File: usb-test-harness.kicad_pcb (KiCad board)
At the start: 4 copper layers, 98 x 85 mm, 92 parts, among them J1 Conn_01x06, J10 USB_A_DUAL, J4 USB_A (female down), J5 Conn_01x03_Male, J6 USB_A_DUAL, J7 USB_A_DUAL, J8 USB_A male UP, J9 USB_B_Micro (up), U1 2k i2c eeprom, U10 NUP4202, U11 NUP4202, U12 NUP4202, U2 SE5120ST33, U3 USB2517, U4 APL3511C, U5 APL3511C, U6 APL3511C, U7 APL3511C, U8 APL3511C, U9 APL3511C, Y1 24MHz

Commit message: last update before changing box design
original box is lovely, and cheap, but only available on TME, so we've
found a new box, Bud CU-388, available on dk and mouser as well, at a
nearly as good price.
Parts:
- moved U10 124.5 mm to (115.2, 66.2)
- moved U11 124.5 mm to (115.2, 70.0)
- moved U12 124.5 mm to (119.5, 66.2)
- moved H5 105.9 mm to (124.9, 66.3)
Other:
- board text added: "github.com/karlp/hubbish rev 2020-03"

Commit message: Updated "finished" for new bud cu-388 box
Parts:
- removed H5: MountingHole, MountingHole:MountingHole_4mm
- moved D1 48.8 mm to (95.2, 57.0)
- moved D2 48.8 mm to (95.2, 55.3)
- moved U10 45.3 mm to (78.2, 40.1)
- moved U12 45.3 mm to (82.5, 40.1)
- moved U11 45.3 mm to (78.2, 44.0)
- moved D9 30.3 mm to (180.8, 94.3)
- moved C21 26.4 mm to (167.8, 95.3)
- moved C30 25.1 mm to (99.7, 97.9), turned to 180 degrees
- moved H4 24.8 mm to (185.3, 105.4)
- moved R10 24.7 mm to (165.0, 59.2), turned to 180 degrees
- moved JP1 24.6 mm to (164.0, 55.0), turned to 180 degrees
- moved H2 24.0 mm to (105.1, 105.4)
- moved J10 23.8 mm to (170.3, 104.4)
- moved U5 23.6 mm to (171.3, 95.3)
- moved U4 23.5 mm to (169.0, 99.2)
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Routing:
- net +5V: track 112.0 -> 41.0 mm
- net +3V3: track 141.1 -> 109.9 mm
- net GNDPWR: track 334.6 -> 306.7 mm, vias 0 -> 1
- net GND: track 67.5 -> 47.1 mm, vias 54 -> 50
- net /upstream-config-leds/CFG_SEL1: track 83.3 -> 98.5 mm, vias 2 -> 0
- net /upstream-config-leds/LED_A3: track 67.1 -> 78.1 mm
- net /upstream-config-leds/~RESET: track 15.5 -> 26.2 mm
- net /upstream-config-leds/LED_A6: track 90.4 -> 80.1 mm
- net /downstream-port-power/OC5: track 93.2 -> 84.0 mm
- net /downstream-port-power/VBUS6: track 17.8 -> 26.9 mm
- net /upstream-config-leds/CFG_SEL1_A: track 9.15 -> 18.2 mm
- net /upstream-config-leds/LA_3-1: track 13.3 -> 4.34 mm
- net /downstream-port-power/EN5: track 97.0 -> 88.1 mm
- net /upstream-config-leds/CFG_SEL2: track 48.7 -> 40.1 mm
- net /downstream-port-power/EN6: track 81.1 -> 74.0 mm
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- removed copper zone on F.Cu, net +5V
- removed copper zone on B.Cu, net GND
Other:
- board size 98 x 85 mm -> 103.6 x 71.8 mm
- board text added: "0"
- board text added: "1"
- board text added: "2"
- board text removed: "2 1 0"

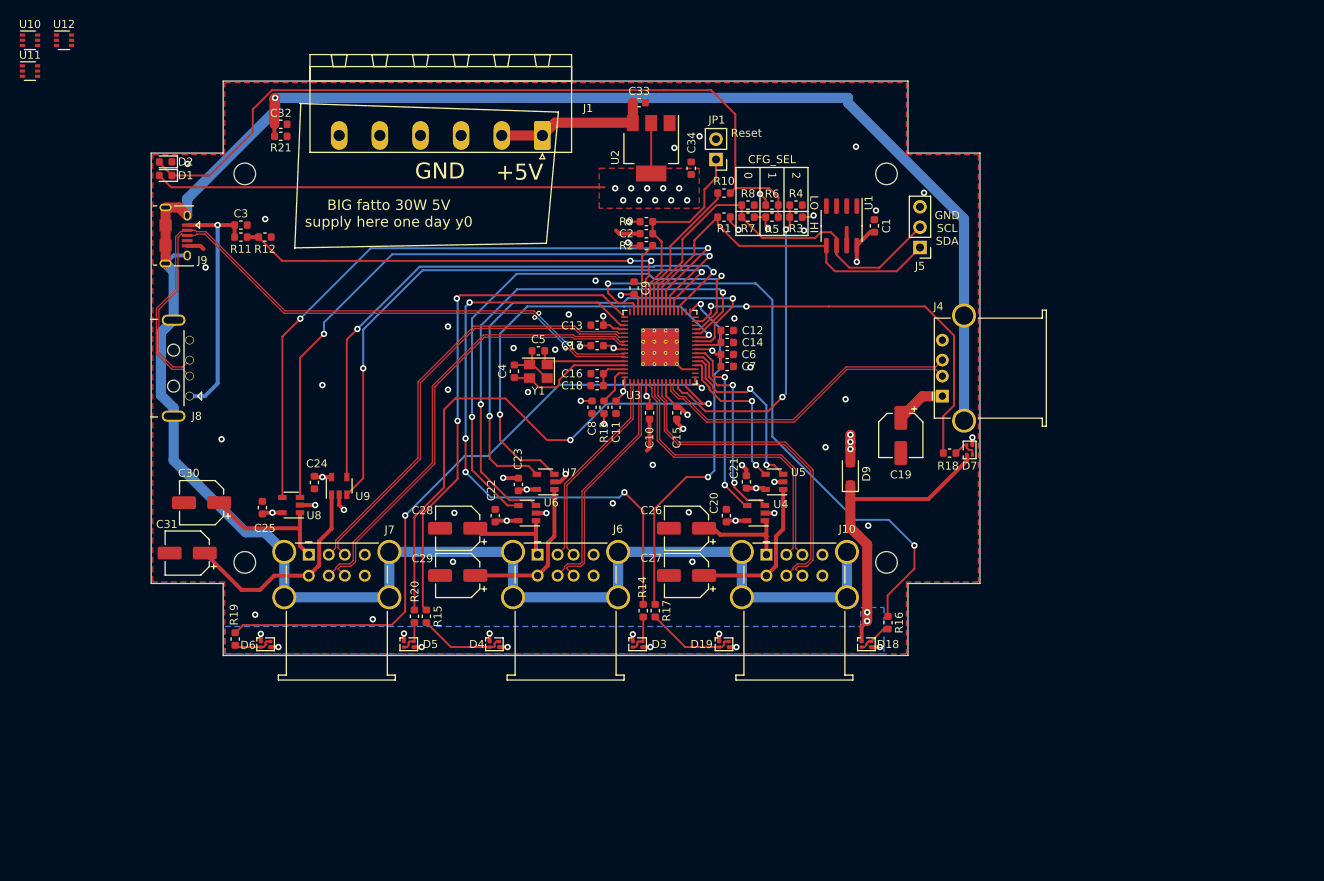
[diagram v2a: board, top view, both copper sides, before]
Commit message: Added esd protection.
Still haven't re-routed the upstream side yet, but nearly.
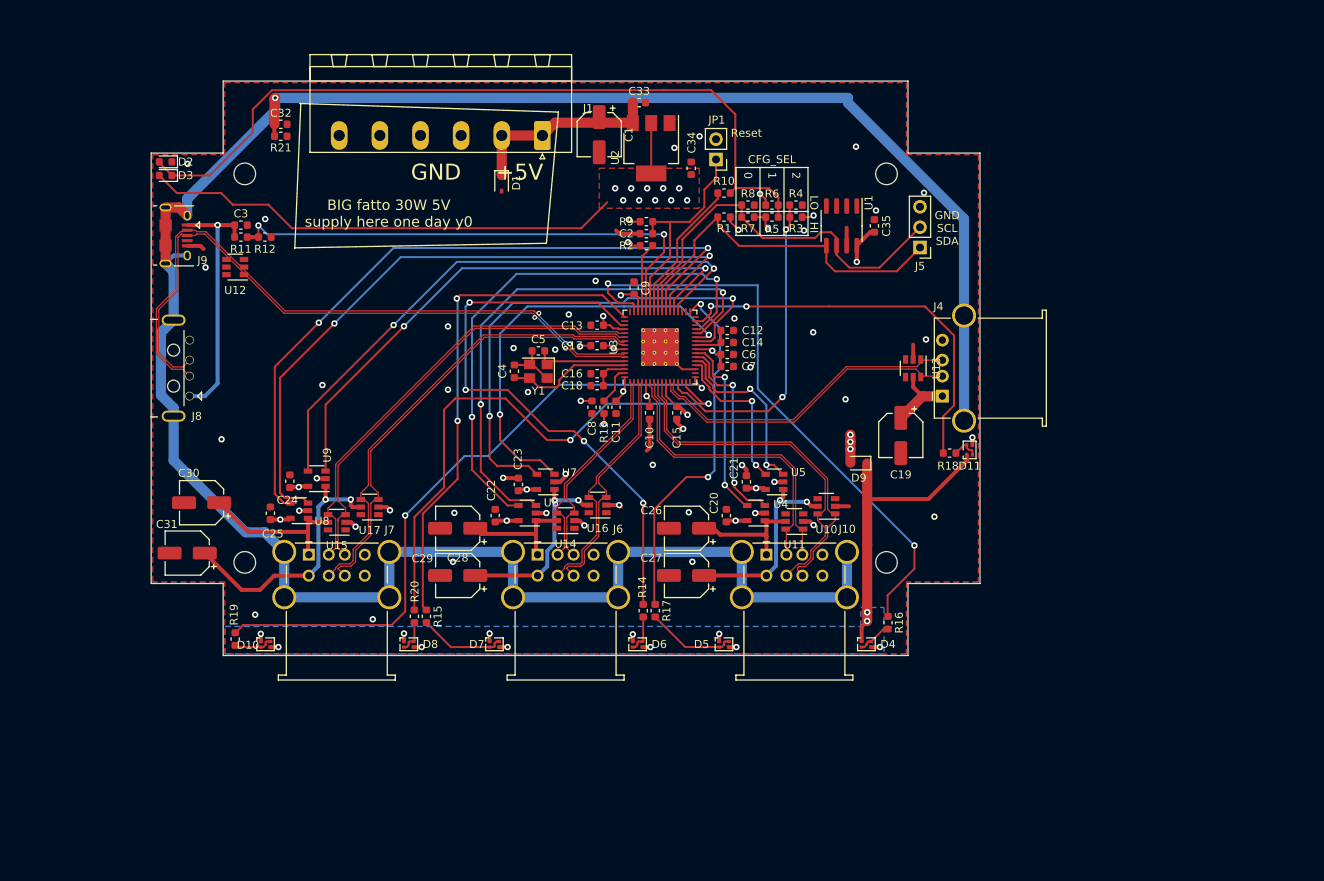
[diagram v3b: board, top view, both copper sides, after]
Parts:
- added C1: 100uF, Capacitor_SMD:CP_Elec_5x5.4, F.Cu at (149.4, 51.9)
- added D1: SD05-7, Diode_SMD:D_SOD-323, F.Cu at (137.2, 57.9)
- added U13: NUP4202, Package_TO_SOT_SMD:SOT-23-6, F.Cu at (188.7, 81.1)
- added U14: NUP4202, Package_TO_SOT_SMD:SOT-23-6, F.Cu at (145.2, 100.2)
- added U15: NUP4202, Package_TO_SOT_SMD:SOT-23-6, F.Cu at (116.6, 100.3)
- added U16: NUP4202, Package_TO_SOT_SMD:SOT-23-6, F.Cu at (149.2, 98.2)
- added U17: NUP4202, Package_TO_SOT_SMD:SOT-23-6, F.Cu at (120.7, 98.5)
- D9: footprint Diode_SMD:D_SOD-123F -> Diode_SMD:D_SOD-323
- U10, U11, U12: footprint Package_TO_SOT_SMD:SOT-363_SC-70-6 -> Package_TO_SOT_SMD:SOT-23-6
- moved U10 115.3 mm to (177.8, 98.3), turned to 180 degrees
- moved U11 110.9 mm to (173.8, 100.2), turned to 180 degrees
- moved U12 35.5 mm to (103.9, 68.5), turned to 180 degrees
- moved C24 3.07 mm to (110.7, 95.2), turned to 90 degrees
- moved U9 2.94 mm to (114.1, 94.9), turned to 180 degrees
- moved D9 1.71 mm to (181.8, 93.0), turned to 180 degrees
- moved C25 1.22 mm to (108.3, 99.2)
- moved U8 1.22 mm to (111.9, 98.9)
- renumbered C1 to C35, D6 to D10, D7 to D11, D1 to D3, D18 to D4, D19 to D5, D3 to D6, D4 to D7, D5 to D8
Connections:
- U10 pad 1: (no net) -> /downstream-port-power/U2+
- U10 pad 2: (no net) -> GND
- U10 pad 5: (no net) -> /downstream-port-power/VBUS2
- U10 pad 6: (no net) -> /downstream-port-power/U2-
- U11 pad 1: (no net) -> /downstream-port-power/U1+
- U11 pad 2: (no net) -> GND
- U11 pad 5: (no net) -> /downstream-port-power/VBUS1
- U11 pad 6: (no net) -> /downstream-port-power/U1-
- U12 pad 1: (no net) -> /upstream-config-leds/UP+
- U12 pad 2: (no net) -> GND
- U12 pad 3: (no net) -> /upstream-config-leds/UP-
- U12 pad 4: (no net) -> /upstream-config-leds/UP-
- U12 pad 5: (no net) -> /upstream-config-leds/VBUS_UP
- U12 pad 6: (no net) -> /upstream-config-leds/UP+
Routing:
- net GND: track 47.1 -> 56.8 mm, vias 50 -> 55
- net +5V: track 41.0 -> 49.7 mm
- net /upstream-config-leds/VBUS_DET: track 58.4 -> 64.8 mm
- net /downstream-port-power/VBUS6: track 26.9 -> 32.9 mm, vias 0 -> 2
- net /upstream-config-leds/LED_A1: track 78.4 -> 72.6 mm
- net /downstream-port-power/VBUS2: track 18.1 -> 23.1 mm, vias 0 -> 2
- net /downstream-port-power/VBUS4: track 19.5 -> 24.0 mm, vias 0 -> 2
- net +3V3: track 109.9 -> 113.9 mm
- net /downstream-port-power/OC5: track 84.0 -> 87.8 mm
- net /downstream-port-power/OC6: track 73.4 -> 69.9 mm
- net /downstream-port-power/U2-: track 41.7 -> 44.8 mm
- net /downstream-port-power/VBUS5: track 17.3 -> 20.1 mm
- net /downstream-port-power/VBUS1: track 11.3 -> 13.9 mm
- net /downstream-port-power/VBUS3: track 12.3 -> 14.8 mm
- net /downstream-port-power/U2+: track 41.7 -> 44.2 mm
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
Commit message: "finished" upstream ESD, silk, text and commentary
Nearly there?
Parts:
- moved U12 4.70 mm to (102.0, 64.2), turned to 90 degrees
- moved R19 4.00 mm to (107.4, 113.0), turned to 180 degrees
- moved C3 3.49 mm to (107.4, 61.0)
- moved R11 3.49 mm to (107.4, 62.5)
- moved R12 3.49 mm to (110.4, 62.5)
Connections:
- U12 pad 1: /upstream-config-leds/UP+ -> (no net)
- U12 pad 3: /upstream-config-leds/UP- -> /upstream-config-leds/UP+
- U12 pad 6: /upstream-config-leds/UP+ -> (no net)
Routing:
- net /upstream-config-leds/LED_A6: track 80.1 -> 75.4 mm
- net /upstream-config-leds/VBUS_UP: track 31.4 -> 36.0 mm
- net GND: track 56.8 -> 60.9 mm, vias 55 -> 58
- net +3V3: track 113.9 -> 111.2 mm
- net /upstream-config-leds/VBUS_DET: track 64.8 -> 62.9 mm
- net /upstream-config-leds/LA_6-6: track 4.98 -> 6.28 mm
- net /upstream-config-leds/UP-: track 84.2 -> 85.4 mm
- net /upstream-config-leds/UP+: track 83.2 -> 84.4 mm
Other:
- board text added: "HiSpeed"
- board text added: "Port 1/2"
- board text added: "Port 3/4"
- board text added: "Port 5"
- board text added: "Port 6/7"
- board text added: "Port LEDs Green: LS Red: FS Orange: HS"
- board text added: "Upstream"

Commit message: more silk and polish tweaks
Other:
- board text removed: "FIX ALL THE FUCKING SILK!"

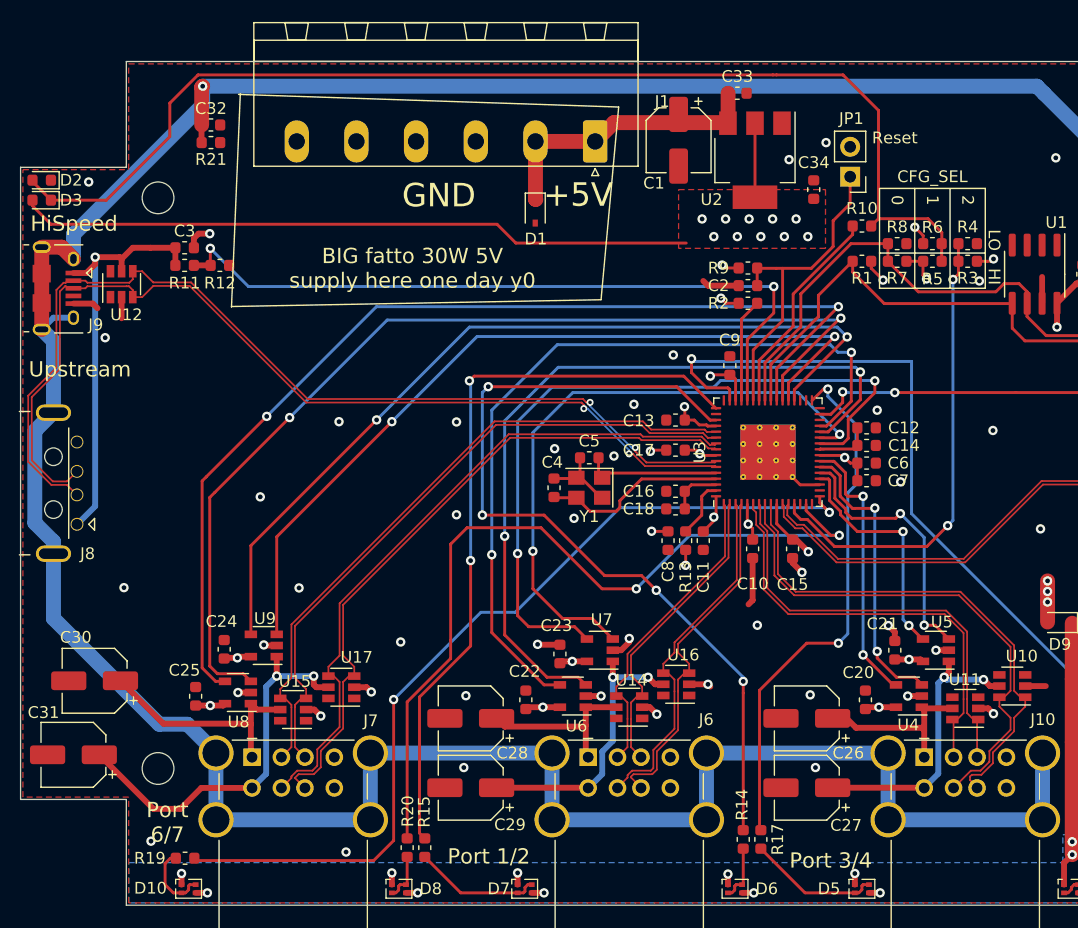
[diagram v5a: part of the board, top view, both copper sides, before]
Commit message: pcb: expand usb hub vias to 0.4mm for cheaper manufacturing
also, added jlc text for pcb order number
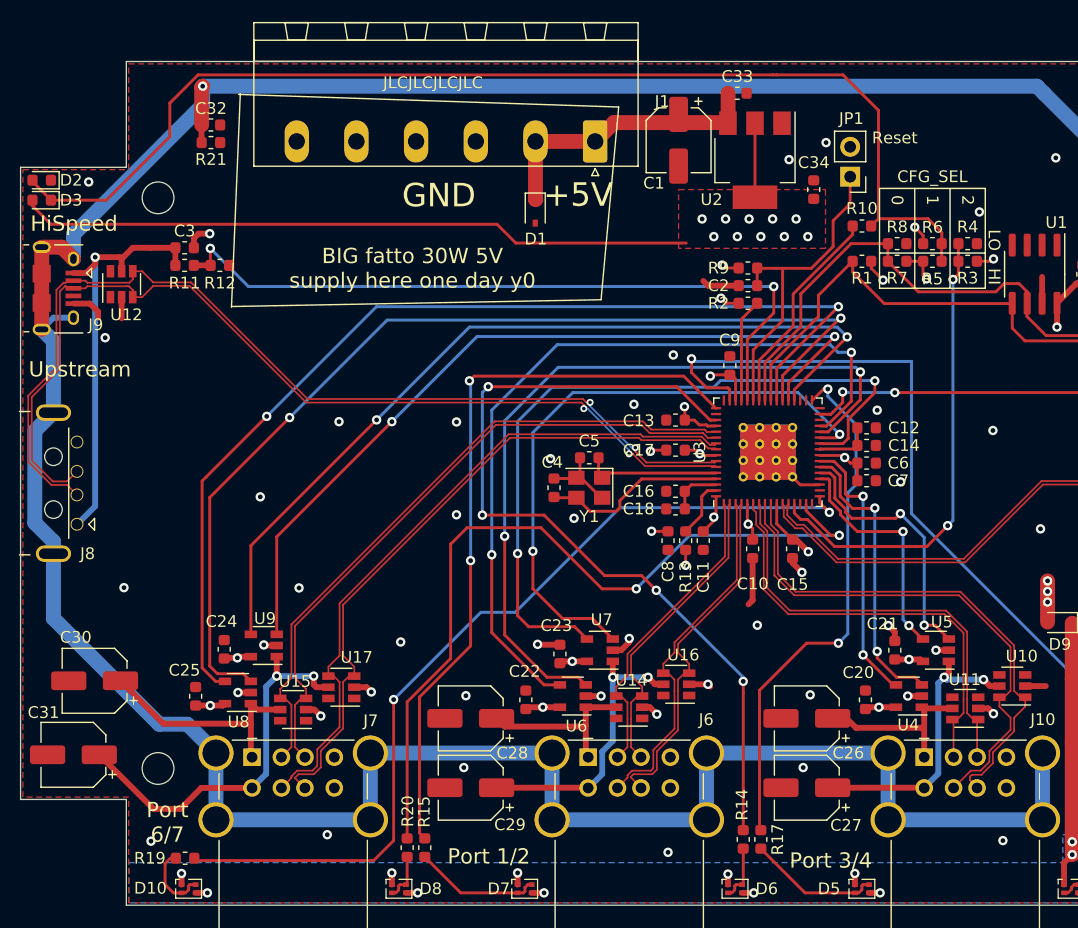
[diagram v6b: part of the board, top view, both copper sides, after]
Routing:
- net GND: track 60.9 -> 61.6 mm, vias 58 -> 59
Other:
- board text added: "JLCJLCJLCJLC"

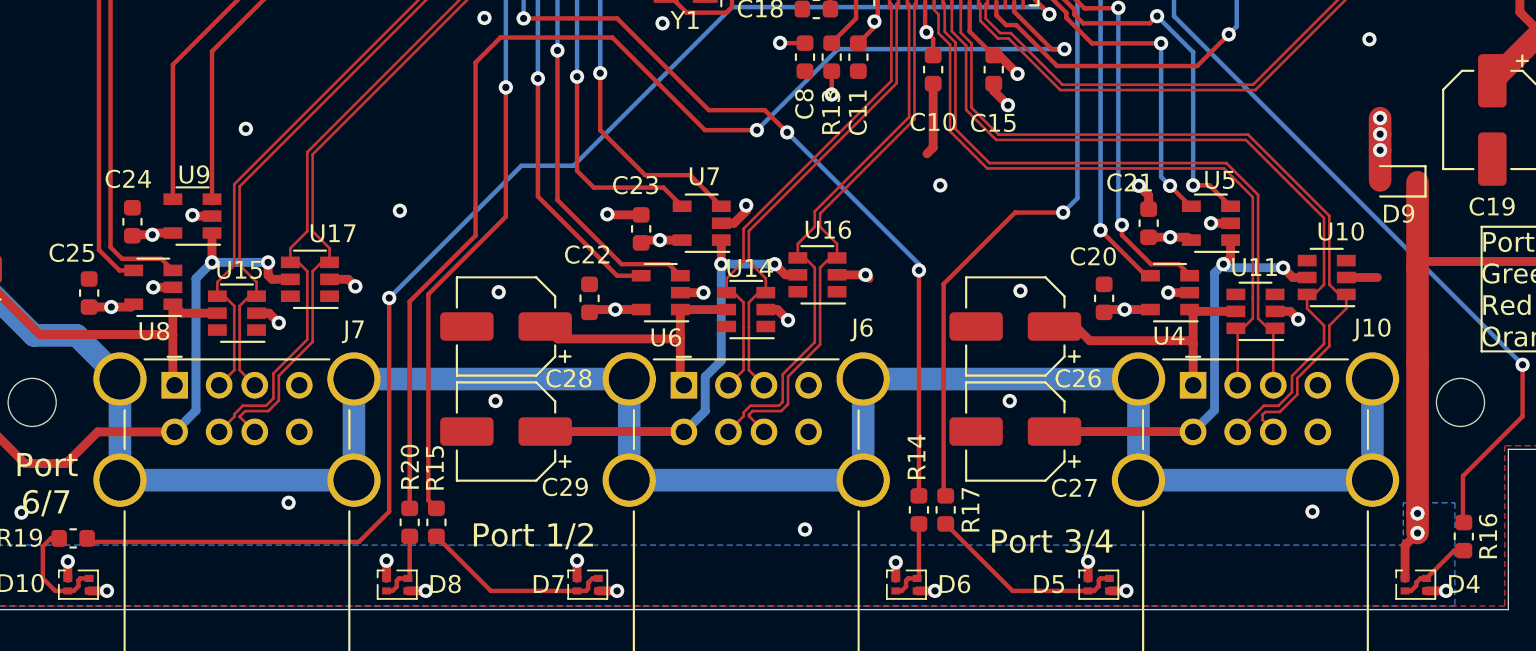
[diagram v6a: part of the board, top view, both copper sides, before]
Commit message: update pcb to latest proj version too
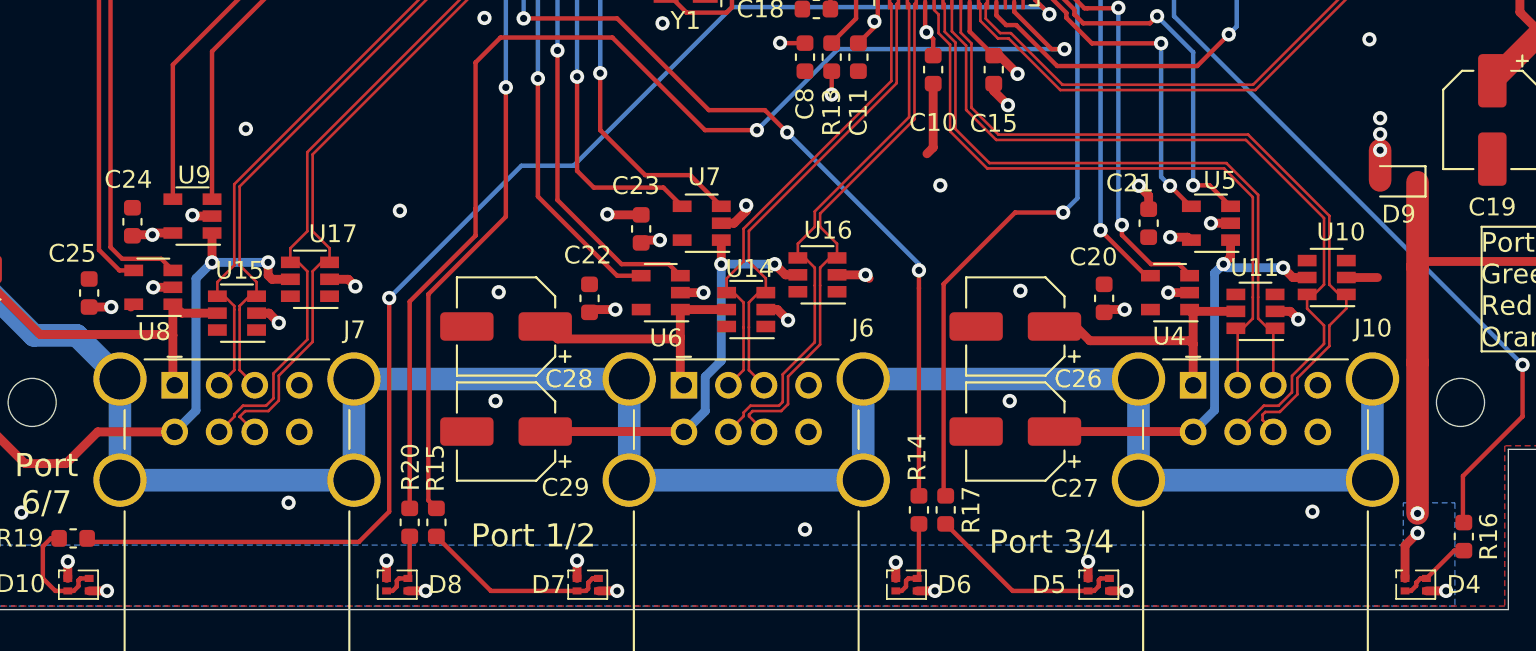
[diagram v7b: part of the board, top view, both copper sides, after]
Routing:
- net +5V: track 49.7 -> 43.2 mm
- net +3V3: track 111.2 -> 109.4 mm
- net /upstream-config-leds/LED_DRIVE: track 42.6 -> 41.5 mm
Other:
- net class Default removed
- net class usb-4l-2313 removed
